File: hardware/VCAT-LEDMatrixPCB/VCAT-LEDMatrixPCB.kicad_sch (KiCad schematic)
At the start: 57 parts, among them J1 Conn_01x03

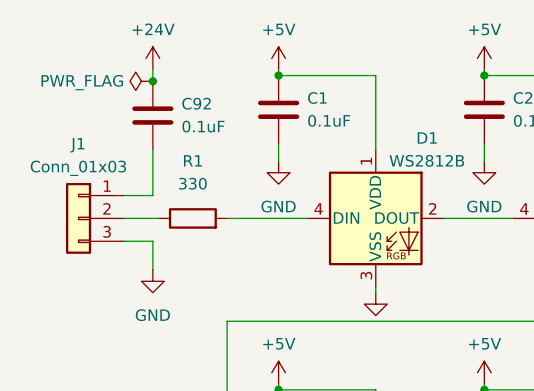
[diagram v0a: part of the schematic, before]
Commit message: Layout 50% done
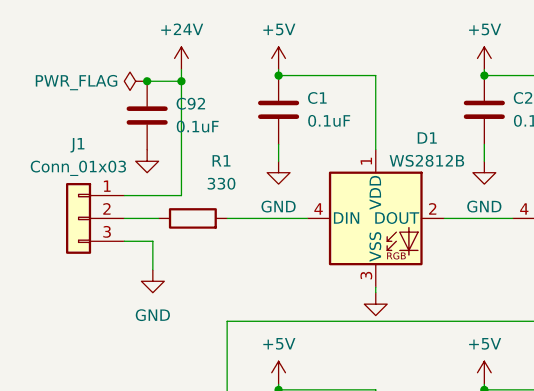
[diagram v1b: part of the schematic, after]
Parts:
- C1, C10, C11, C12, C13, C14, C15, C16, C17, C18, C19, C2, C20, C21, C22, C23, C24, C25, C26, C27, C3, C4, C5, C6, C7, C8, C9, C92: footprint Capacitor_SMD:C_0603_1608Metric_Pad1.08x0.95mm_HandSolder -> Capacitor_SMD:C_0603_1608Metric
- R1: footprint Resistor_SMD:R_0201_0603Metric_Pad0.64x0.40mm_HandSolder -> Resistor_SMD:R_0603_1608Metric
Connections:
- net +24V: now also J1.1 (Pin_1)
- net GND: now also C92.2
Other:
- moved on the sheet: C92
